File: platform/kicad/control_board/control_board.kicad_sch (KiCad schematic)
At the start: 46 parts, among them J1 DHT22, J10 ADC1,7, J11 Qwiic JST, J12 Qwiic JST, J13 PJ-002A, J14 ROUTER 24V, J2 DS18B20, J4 24V IN, J5 USB_PWR_IN, J7 24V/5V OUT, J8 Nav Light, J8 UART, J9 ADC1,6, K1 LCA717, K2 LCA717, K3 LCA717, K4 LCA717, U1 ESP32-DevKitC, U2 ACS722xLCTR-20AU

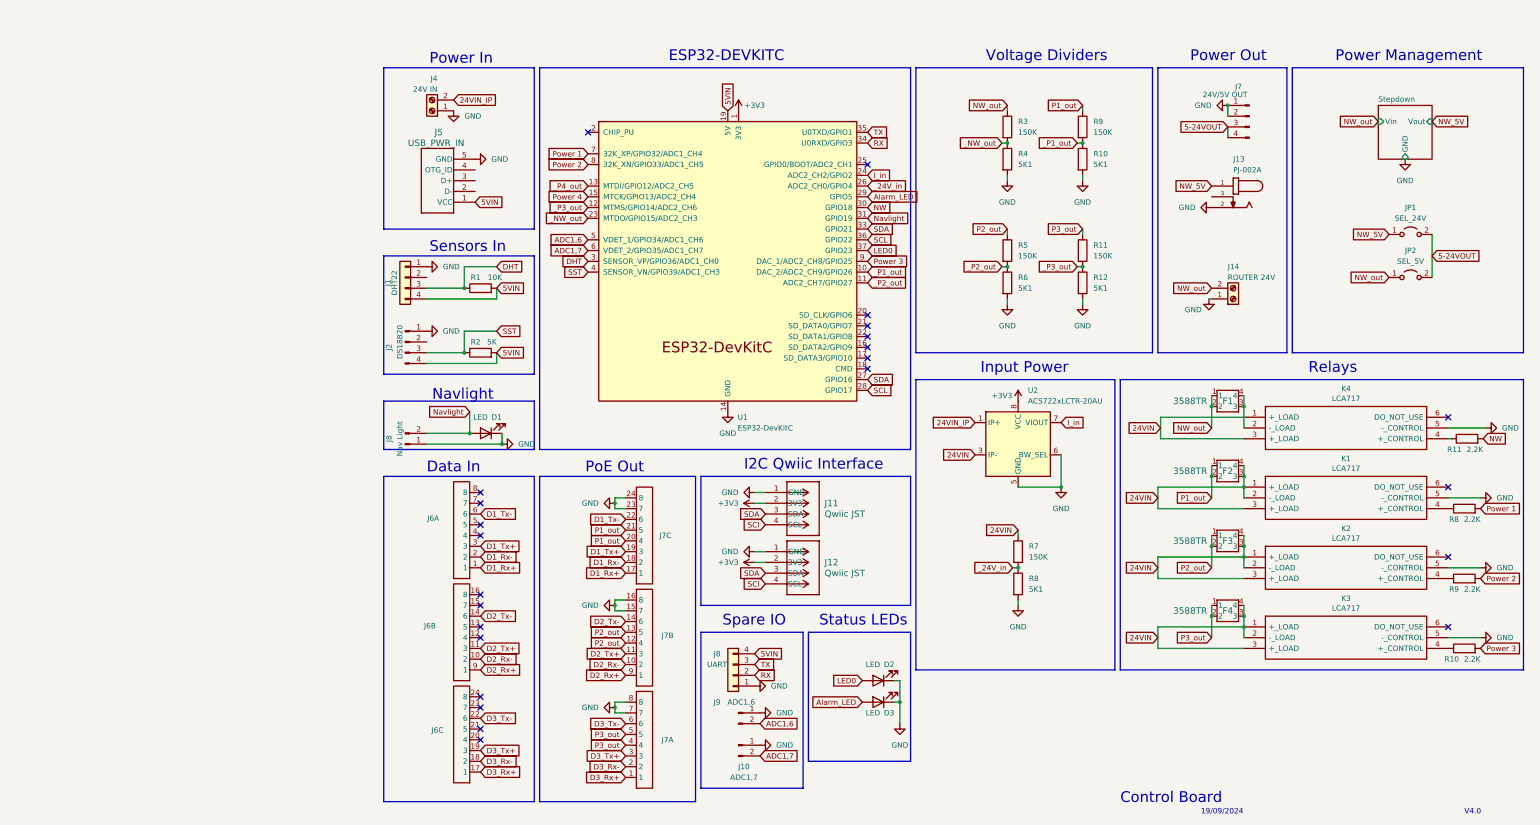
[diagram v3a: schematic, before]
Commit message: Update Control Board layout
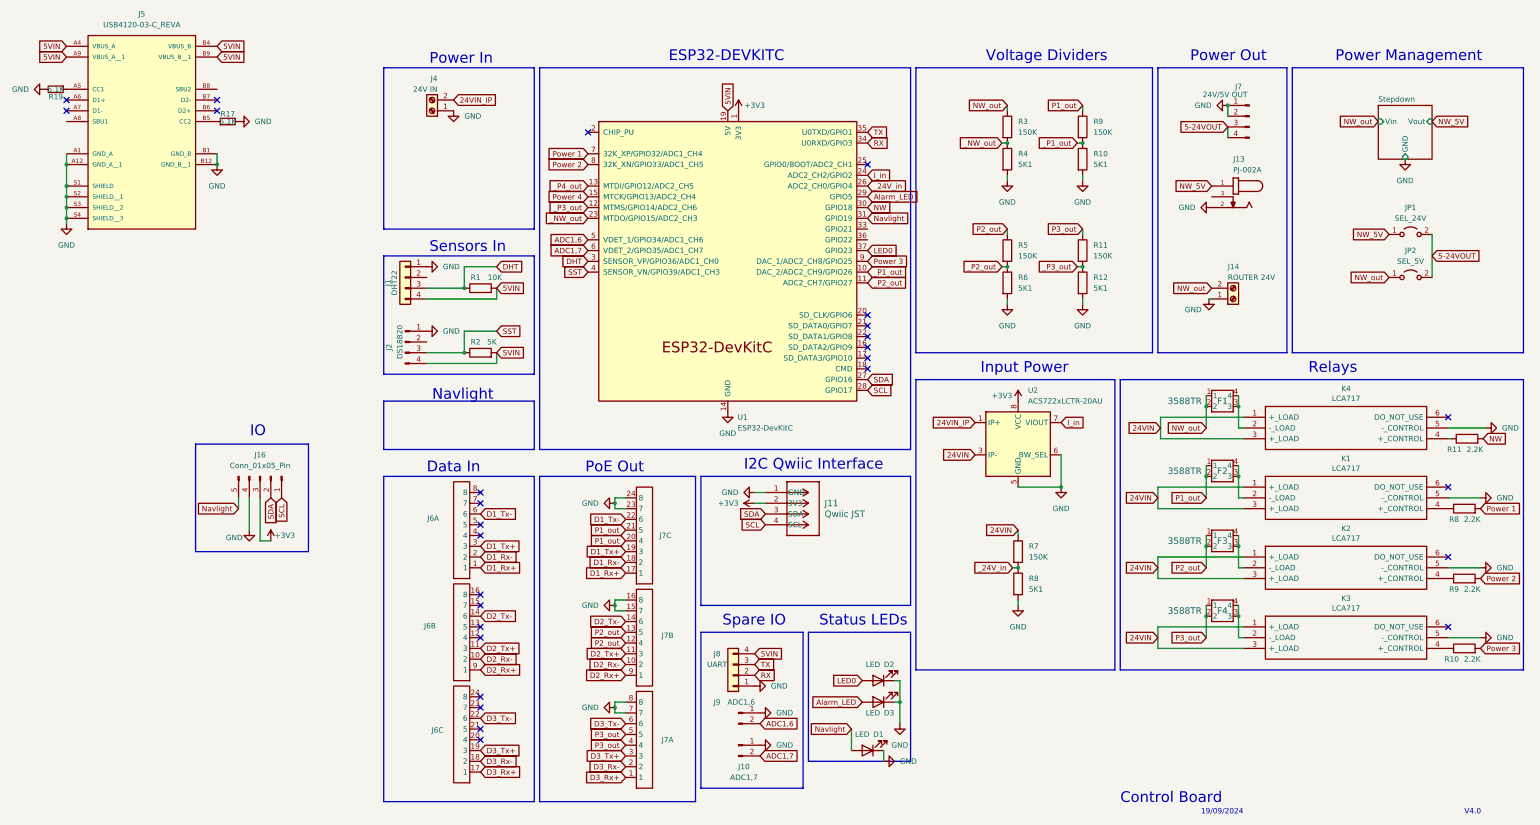
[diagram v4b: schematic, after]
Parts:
- removed J12: Qwiic JST, AusOcean:CONN_SM04B-SRSS-TB_JST, symbol AusOcean:Qwiic JST
- removed J5: USB_PWR_IN, AusOcean:USB_Micro_B_CONN, symbol AusOcean:USB_Micro_B_2.0
- removed J8: Nav Light, Connector_JST:JST_EH_B2B-EH-A_1x02_P2.50mm_Vertical, symbol AusOceanPCB-rescue:Conn_01x02_Male-Connector
- added J16: Conn_01x05_Pin, Connector_JST:JST_SH_SM05B-SRSS-TB_1x05-1MP_P1.00mm_Horizontal, symbol Connector:Conn_01x05_Pin
- added J5: USB4120-03-C_REVA, AusOcean:GCT_USB4120-03-C_REVA, symbol AusOcean:USB4120-03-C_REVA
- added R17, R19: 5.1K, Resistor_SMD:R_0201_0603Metric, symbol Device:R_Small
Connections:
- net SCl is gone; now on net SCL: J11.4 (SCL)
- net +3V3: now also J16.3 (Pin_3)
- net 24VIN: no longer F2.3, F2.4, F3.3, F3.4, F4.3, F4.4, K1.2 (-_LOAD), K2.2 (-_LOAD), K3.2 (-_LOAD)
- net 5VIN: now also J5.A4 (VBUS_A), J5.A9 (VBUS_A__1), J5.B4 (VBUS_B), J5.B9 (VBUS_B__1)
- net GND: now also J16.4 (Pin_4), J5.A1 (GND_A), J5.A12 (GND_A__1), J5.B1 (GND_B), J5.B12 (GND_B__1), J5.S1 (SHIELD), J5.S2 (SHIELD__1), J5.S3 (SHIELD__2), J5.S4 (SHIELD__3), R17.2, R19.2
- net Navlight: now also J16.5 (Pin_5)
- net SCL: now also J16.1 (Pin_1); no longer U1.36 (GPIO22)
- net SDA: now also J16.2 (Pin_2); no longer U1.33 (GPIO21)
- new net: F3.3, F3.4, K2.2 (-_LOAD)
- new net: J5.A5 (CC1), R19.1
- new net: F2.3, F2.4, K1.2 (-_LOAD)
- new net: J5.B5 (CC2), R17.1
- new net: F4.3, F4.4, K3.2 (-_LOAD)
- no-connect marks 24 -> 28
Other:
- note added: "IO"
- moved on the sheet: D1, F1, F3

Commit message: Controller: Finalise Layout and Labelling (#3)
This change finalises the layout and tracks for the controller PCB, as well as the labelling.
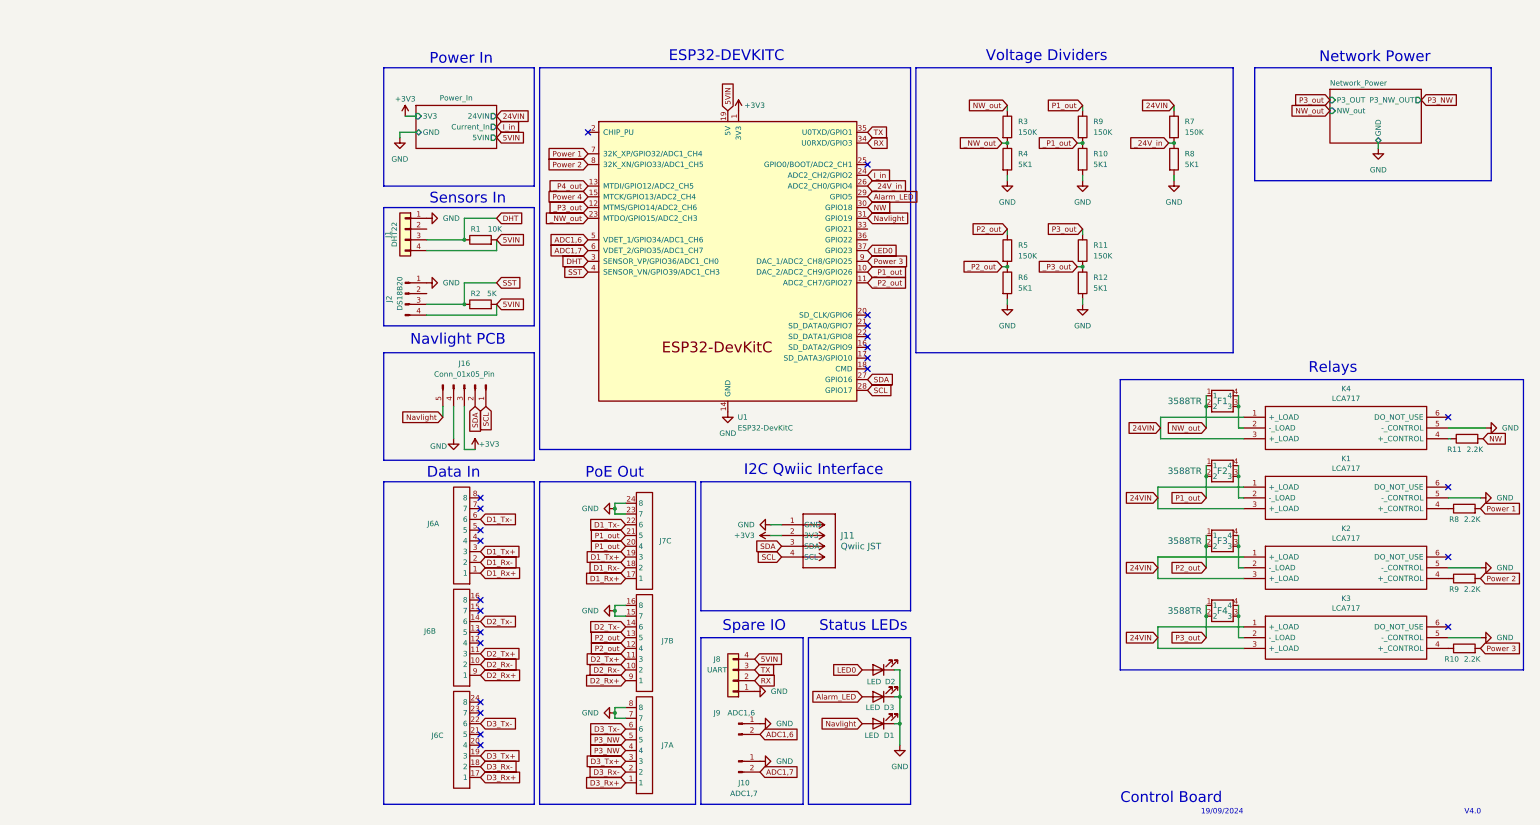
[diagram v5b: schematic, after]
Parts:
- removed J13: PJ-002A, AusOcean:CUI_PJ-002A, symbol AusOcean:PJ-002A
- removed J14: ROUTER 24V, AusOcean:CUI_Screw_terminal_1x2, symbol Connector:Screw_Terminal_01x02
- removed J4: 24V IN, AusOcean:CUI_Screw_terminal_1x2, symbol Connector:Screw_Terminal_01x02
- removed J5: USB4120-03-C_REVA, AusOcean:GCT_USB4120-03-C_REVA, symbol AusOcean:USB4120-03-C_REVA
- removed J7: 24V/5V OUT, Connector_JST:JST_EH_B4B-EH-A_1x04_P2.50mm_Vertical, symbol AusOceanPCB-rescue:Conn_01x04_Male-Connector
- removed JP1: SEL_24V, Jumper:SolderJumper-2_P1.3mm_Open_TrianglePad1.0x1.5mm, symbol Jumper:Jumper_2_Open
- removed JP2: SEL_5V, Jumper:SolderJumper-2_P1.3mm_Open_TrianglePad1.0x1.5mm, symbol Jumper:Jumper_2_Open
- removed R17, R19: 5.1K, Resistor_SMD:R_0201_0603Metric, symbol Device:R_Small
- removed U2: ACS722xLCTR-20AU, Package_SO:SOIC-8_3.9x4.9mm_P1.27mm, symbol Sensor_Current:ACS722xLCTR-20AU
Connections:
- net P3_out: no longer J7.4, J7.5
- new net P3_NW: J7.4, J7.5
- no-connect marks 28 -> 24
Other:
- removed sheet Stepdown
- added sheet Network_Power (network_power.kicad_sch)
- added sheet Power_In (power_in.kicad_sch)
- note added: "Navlight PCB"
- note added: "Network Power"
- note removed: "IO"
- note removed: "Input Power"
- note removed: "Navlight"
- note removed: "Power Management"
- note removed: "Power Out"
- moved on the sheet: D1, D2, D3, J1, J10, J11, J16, J2, J6A, J6B, J6C, J7A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

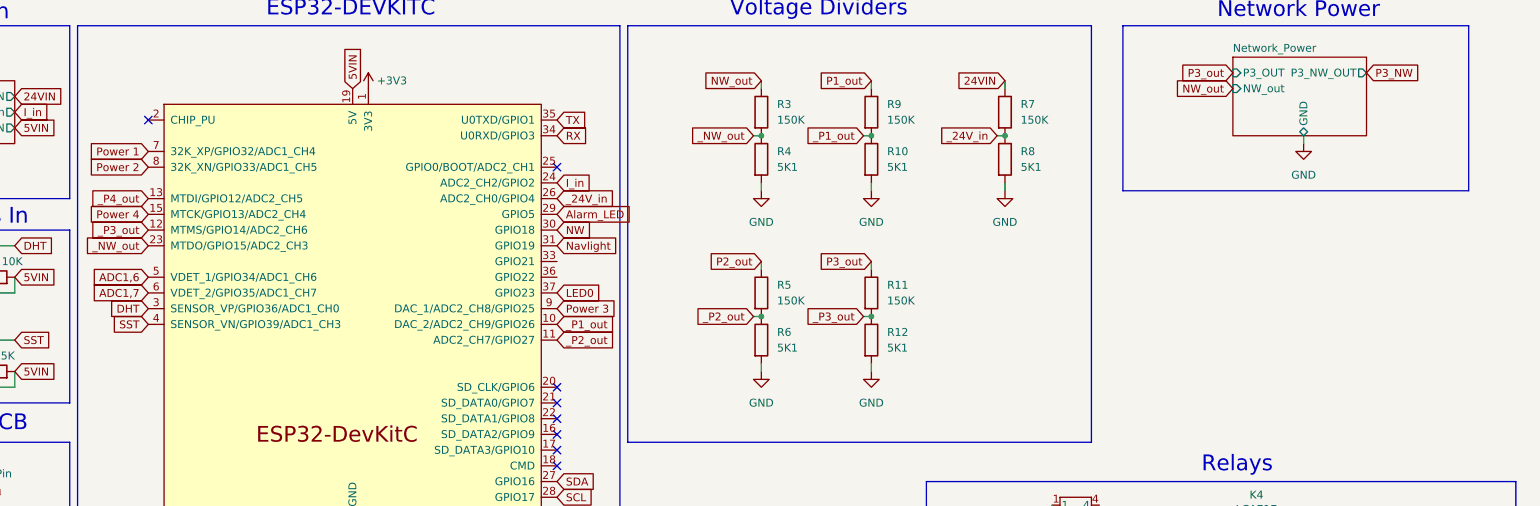
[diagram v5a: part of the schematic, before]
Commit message: Controller: Add External Watchdog (#3)
This change adds a STWD100YNYWY3F watchdog circuit which will be used to
trigger a reset if the ESP does not 'pat' it.
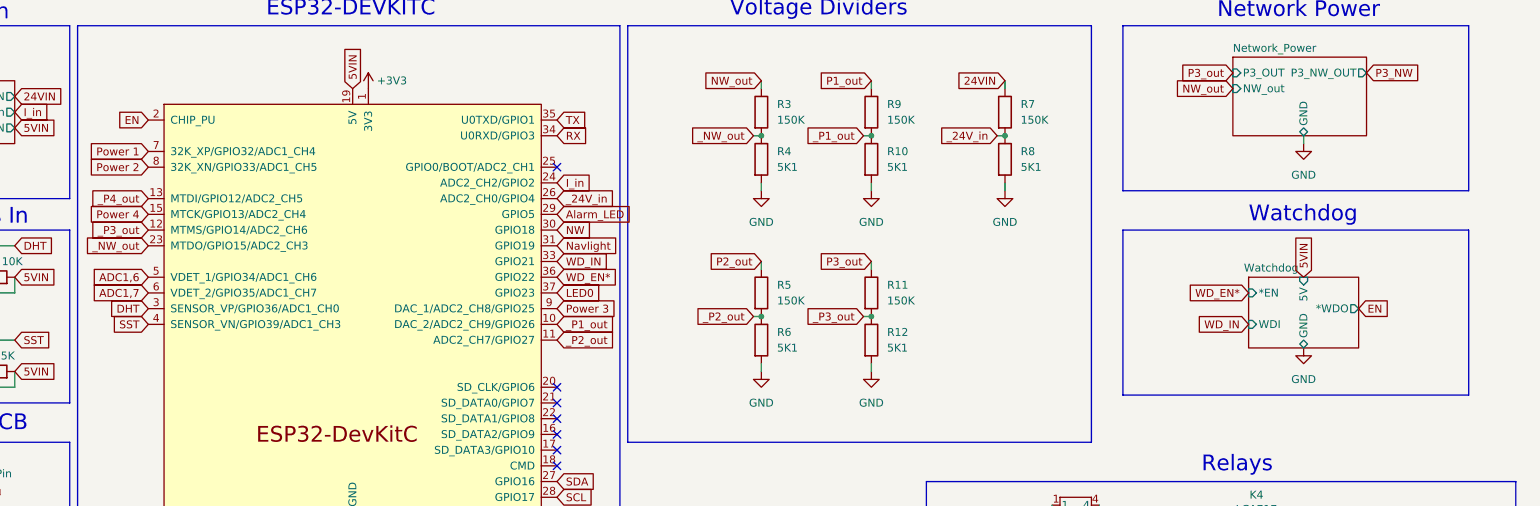
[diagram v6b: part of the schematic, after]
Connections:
- net EN: now reaches U1.2 (CHIP_PU)
- net WD_IN: now reaches U1.33 (GPIO21)
- net WD_EN*: now reaches U1.36 (GPIO22)
- no-connect marks 24 -> 23
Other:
- added sheet Watchdog (watchdog.kicad_sch)
- note added: "Watchdog"

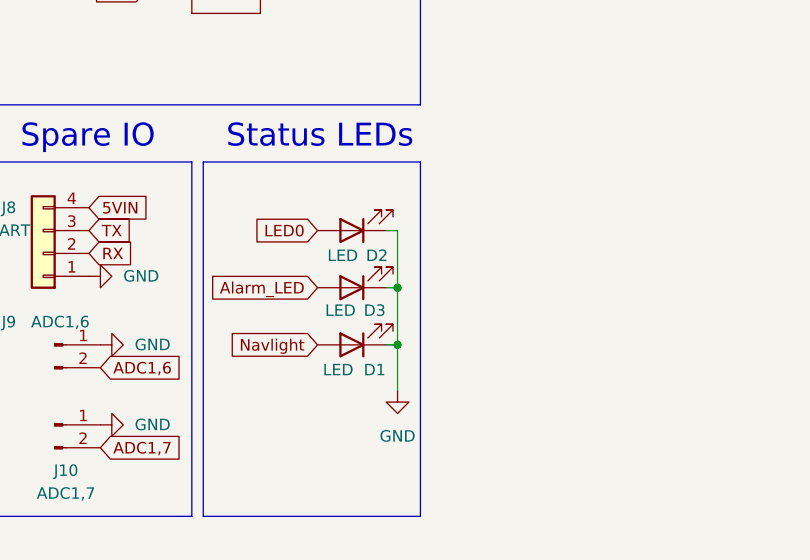
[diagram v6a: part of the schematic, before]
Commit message: Control Board: Finalise V4 Rev A
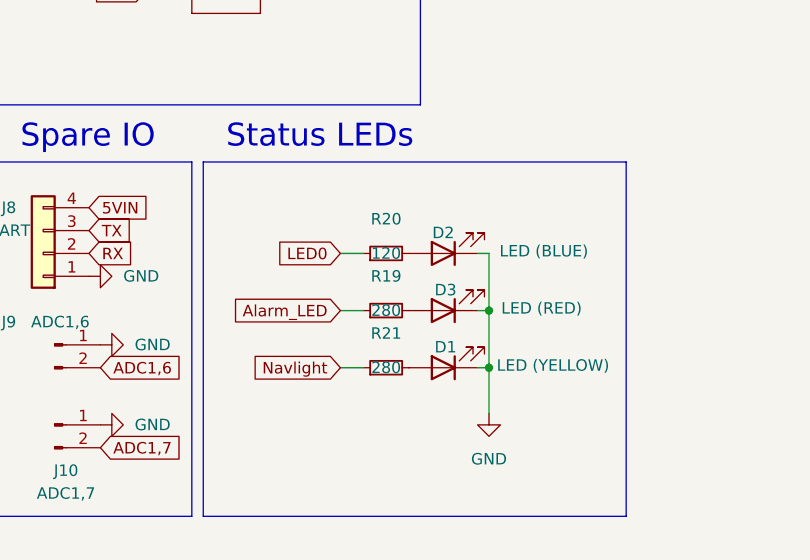
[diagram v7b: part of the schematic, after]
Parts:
- added R19, R21: 280, Resistor_SMD:R_0201_0603Metric, symbol Device:R_Small
- added R20: 120, Resistor_SMD:R_0201_0603Metric, symbol Device:R_Small
- D1: value LED -> LED (YELLOW)
- D2: value LED -> LED (BLUE)
- D3: value LED -> LED (RED)
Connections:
- net Alarm_LED: now also R19.1; no longer D3.2 (A)
- net LED0: now also R20.1; no longer D2.2 (A)
- net Navlight: now also R21.1; no longer D1.2 (A)
- new net: D2.2 (A), R20.2
- new net: D1.2 (A), R21.2
- new net: D3.2 (A), R19.2
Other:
- moved on the sheet: D1, D2, D3
